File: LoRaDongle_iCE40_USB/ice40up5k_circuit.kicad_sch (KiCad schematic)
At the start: 28 parts, among them IC2 ICE40UP5K-UWG30ITR1K, IC3 N25Q032A13ESC40F, J3 Conn_02x02_Top_Bottom, J6 Conn_01x06, J7 Jumper_NC_Small, J9 Conn_02x02_Top_Bottom, SW1 SW_Push, X1 ECS-2520MV-500-BL-TR

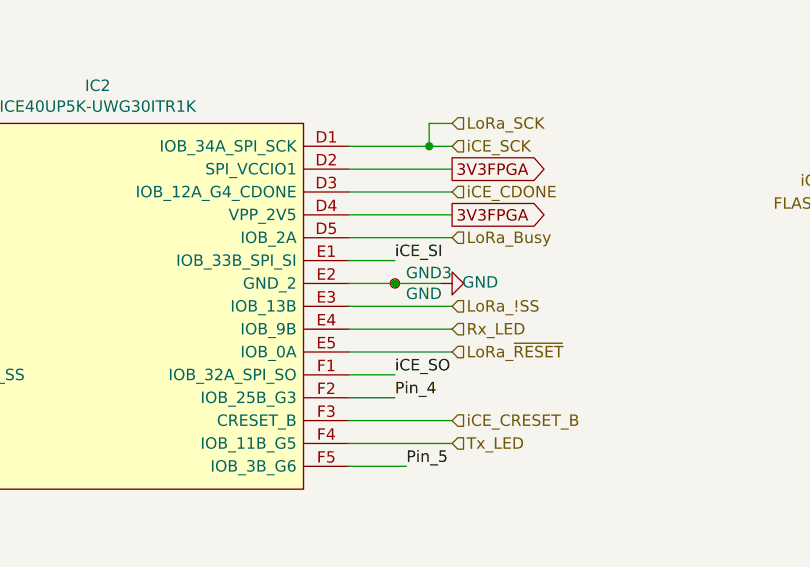
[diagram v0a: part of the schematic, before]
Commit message: added copper pours
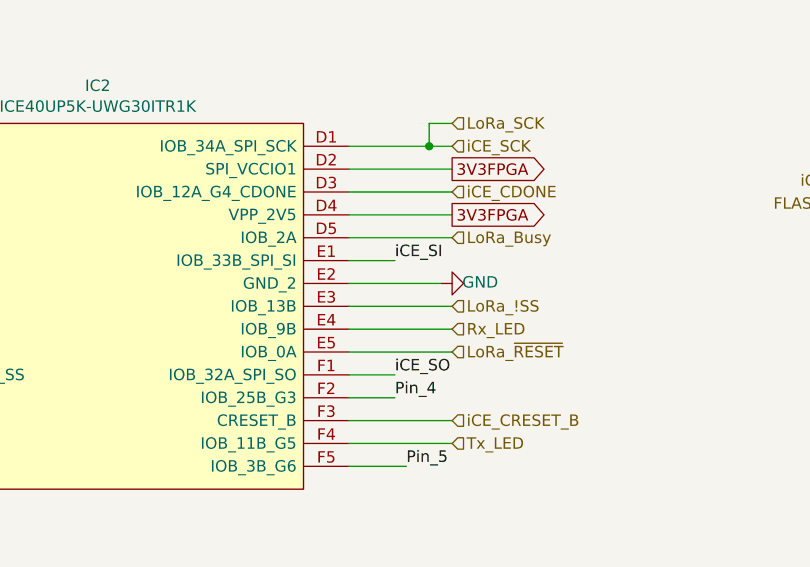
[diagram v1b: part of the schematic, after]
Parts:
- removed GND3: GND, TestPoint:TestPoint_Pad_D1.0mm, symbol Connector:TestPoint_Small
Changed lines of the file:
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@@
   (junction (at 120.65 38.1) (diameter 0) (color 0 0 0 0)
-  )
-  (junction (at 128.27 90.17) (diameter 0) (color 0 0 0 0)
   )
   (junction (at 165.1 39.37) (diameter 0) (color 0 0 0 0)
@@
     (stroke (width 0) (type default) (color 0 0 0 0))
   )
-  (wire (pts (xy 123.19 90.17) (xy 128.27 90.17))
+  (wire (pts (xy 123.19 90.17) (xy 133.35 90.17))
     (stroke (width 0) (type default) (color 0 0 0 0))
   )
@@
   )
   (wire (pts (xy 140.97 157.48) (xy 140.97 153.67))
-    (stroke (width 0) (type default) (color 0 0 0 0))
-  )
-  (wire (pts (xy 128.27 90.17) (xy 133.35 90.17))
     (stroke (width 0) (type default) (color 0 0 0 0))
   )
@@
     (pin "2")
   )
-  (symbol (lib_id "Connector:TestPoint_Small") (at 128.27 90.17 0) (unit 1)
-    (in_bom yes) (on_board yes)
-    (property "Reference" "GND3" (id 0) (at 129.4892 89.0016 0)
-      (effects (font (size 1.27 1.27)) (justify left))
-    )
-    (property "Value" "GND" (id 1) (at 129.4892 91.313 0)
-      (effects (font (size 1.27 1.27)) (justify left))
-    )
-    (property "Footprint" "TestPoint:TestPoint_Pad_D1.0mm" (id 2) (at 133.35 90.17 0)
-      (effects (font (size 1.27 1.27)) hide)
-    )
-    (property "Datasheet" "~" (id 3) (at 133.35 90.17 0)
-      (effects (font (size 1.27 1.27)) hide)
-    )
-    (pin "1")
-  )
 )

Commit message: updating symbol details
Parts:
- C23, C24, C25, C26, C27, C29, C30, C31, C32: Manufacturer (none) -> Murata Electronics; Manufacturer Part Number (none) -> GRM155R71C104KA88D; Package (none) -> 0402; Type (none) -> SMD
- C28: Manufacturer (none) -> Murata Electronics; Manufacturer Part Number (none) -> GRM155R70J105MA12D; Package (none) -> 0402; Type (none) -> SMD
- IC2: Manufacturer (none) -> Lattice Semiconductor; Manufacturer Part Number (none) -> ICE40UP5K-UWG30ITR1K; Package (none) -> 30-UFBGA, WLCSP; Type (none) -> SMD
- J3, J6, J7, J9: Manufacturer (none) -> -; Manufacturer Part Number (none) -> -; Package (none) -> -; Type (none) -> Through Hole
- SW1: Manufacturer (none) -> (none); Type (none) -> Through Hole
- X1: Manufacturer (none) -> ECS Inc.; Manufacturer Part Number (none) -> ECS-2520MV-500-BL-TR; Package (none) -> 4 Pin Crystal; Type (none) -> SMD
- iCE_SI1, iCE_SO1: Manufacturer (none) -> -; Manufacturer Part Number (none) -> -; Package (none) -> -; Type (none) -> -

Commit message: updated BOM
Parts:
- D2: Manufacturer (none) -> SunLED; Manufacturer Part Number (none) -> XZVG53W-8; Package (none) -> 0603
- R13, R14, R15, R16, R17: Manufacturer (none) -> Stackpole Electronics Inc; Manufacturer Part Number (none) -> RMCF0402FT10K0
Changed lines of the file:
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@@
+      (effects (font (size 1.27 1.27)) hide)
+    )
+    (property "Description" "RES 10K OHM 1% 1/16W 0402" (id 4) (at 153.67 149.86 0)
+      (effects (font (size 1.27 1.27)) hide)
+    )
+    (property "Manufacturer" "Stackpole Electronics Inc" (id 5) (at 153.67 149.86 0)
+      (effects (font (size 1.27 1.27)) hide)
+    )
+    (property "Manufacturer Part Number" "RMCF0402FT10K0" (id 6) (at 153.67 149.86 0)
       (effects (font (size 1.27 1.27)) hide)
     )
@@
       (effects (font (size 1.27 1.27)) hide)
     )
+    (property "Description" "LED GREEN CLEAR CHIP SMD" (id 4) (at 140.97 166.37 0)
+      (effects (font (size 1.27 1.27)) hide)
+    )
+    (property "Manufacturer" "SunLED" (id 5) (at 140.97 166.37 0)
+      (effects (font (size 1.27 1.27)) hide)
+    )
+    (property "Manufacturer Part Number" "XZVG53W-8" (id 6) (at 140.97 166.37 0)
+      (effects (font (size 1.27 1.27)) hide)
+    )
+    (property "Package" "0603" (id 7) (at 140.97 166.37 0)
+      (effects (font (size 1.27 1.27)) hide)
+    )
     (pin "1")
     (pin "2")
@@
       (effects (font (size 1.27 1.27)) hide)
     )
+    (property "Description" "RES 10K OHM 1% 1/16W 0402" (id 4) (at 255.27 74.93 0)
+      (effects (font (size 1.27 1.27)) hide)
+    )
+    (property "Manufacturer" "Stackpole Electronics Inc" (id 5) (at 255.27 74.93 0)
+      (effects (font (size 1.27 1.27)) hide)
+    )
+    (property "Manufacturer Part Number" "RMCF0402FT10K0" (id 6) (at 255.27 74.93 0)
+      (effects (font (size 1.27 1.27)) hide)
+    )
     (pin "1")
     (pin "2")
@@
       (effects (font (size 1.27 1.27)) hide)
     )
+    (property "Description" "RES 10K OHM 1% 1/16W 0402" (id 4) (at 250.19 74.93 0)
+      (effects (font (size 1.27 1.27)) hide)
+    )
+    (property "Manufacturer" "Stackpole Electronics Inc" (id 5) (at 250.19 74.93 0)
+      (effects (font (size 1.27 1.27)) hide)
+    )
+    (property "Manufacturer Part Number" "RMCF0402FT10K0" (id 6) (at 250.19 74.93 0)
+      (effects (font (size 1.27 1.27)) hide)
+    )
     (pin "1")
     (pin "2")
@@
       (effects (font (size 1.27 1.27)) hide)
     )
+    (property "Description" "RES 10K OHM 1% 1/16W 0402" (id 4) (at 191.77 83.82 0)
+      (effects (font (size 1.27 1.27)) hide)
+    )
+    (property "Manufacturer" "Stackpole Electronics Inc" (id 5) (at 191.77 83.82 0)
+      (effects (font (size 1.27 1.27)) hide)
+    )
+    (property "Manufacturer Part Number" "RMCF0402FT10K0" (id 6) (at 191.77 83.82 0)
+      (effects (font (size 1.27 1.27)) hide)
+    )
     (pin "1")
     (pin "2")
@@
       (effects (font (size 1.27 1.27)) hide)
     )
+    (property "Description" "RES 10K OHM 1% 1/16W 0402" (id 4) (at 198.12 69.85 0)
+      (effects (font (size 1.27 1.27)) hide)
+    )
+    (property "Manufacturer" "Stackpole Electronics Inc" (id 5) (at 198.12 69.85 0)
+      (effects (font (size 1.27 1.27)) hide)
+    )
+    (property "Manufacturer Part Number" "RMCF0402FT10K0" (id 6) (at 198.12 69.85 0)
+      (effects (font (size 1.27 1.27)) hide)
+    )

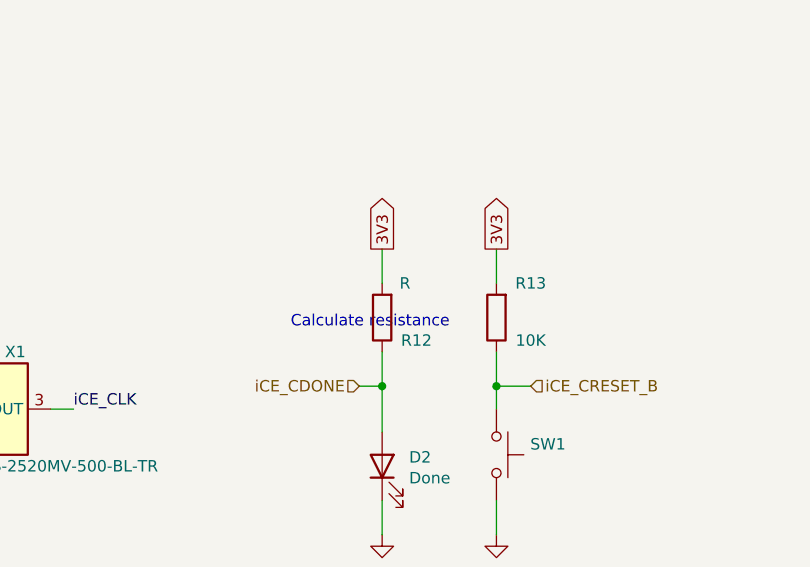
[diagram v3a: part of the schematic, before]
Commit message: generate raw bom csv from kicad
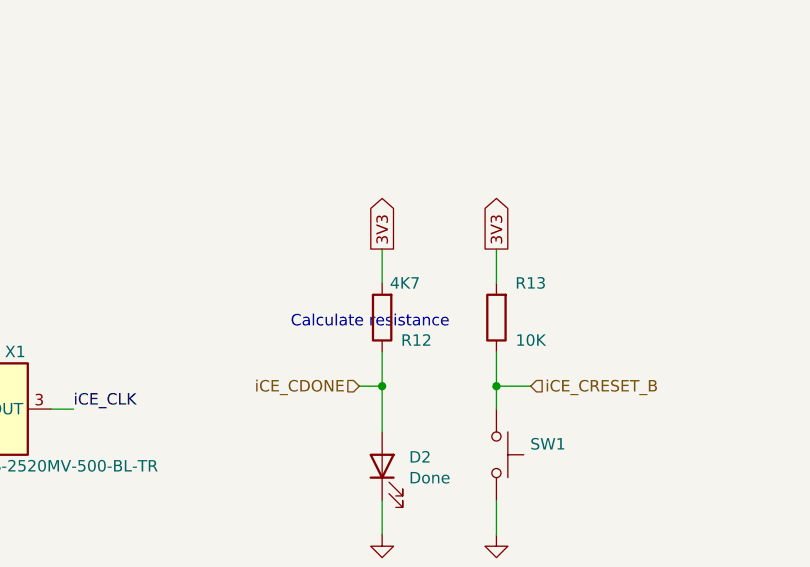
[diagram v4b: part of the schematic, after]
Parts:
- R12: value R -> 4K7; Manufacturer (none) -> Stackpole Electronics Inc; Manufacturer Part Number (none) -> RMCF0402JT4K70; Package (none) -> 0402
- R13, R14, R15, R16, R17: Package (none) -> 0402
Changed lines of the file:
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@@
+      (effects (font (size 1.27 1.27)) hide)
+    )
+    (property "Package" "0402" (id 7) (at 153.67 149.86 0)
       (effects (font (size 1.27 1.27)) hide)
     )
@@
     (in_bom yes) (on_board yes)
     (property "Reference" "R12" (id 0) (at 144.78 152.4 0))
-    (property "Value" "R" (id 1) (at 143.51 146.05 0))
+    (property "Value" "4K7" (id 1) (at 143.51 146.05 0))
     (property "Footprint" "Resistor_SMD:R_0402_1005Metric_Pad0.72x0.64mm_HandSolder" (id 2) (at 142.748 149.86 90)
       (effects (font (size 1.27 1.27)) hide)
     )
     (property "Datasheet" "~" (id 3) (at 140.97 149.86 0)
+      (effects (font (size 1.27 1.27)) hide)
+    )
+    (property "Description" "RES 10K OHM 1% 1/16W 0402" (id 4) (at 140.97 149.86 0)
+      (effects (font (size 1.27 1.27)) hide)
+    )
+    (property "Manufacturer" "Stackpole Electronics Inc" (id 5) (at 140.97 149.86 0)
+      (effects (font (size 1.27 1.27)) hide)
+    )
+    (property "Manufacturer Part Number" "RMCF0402JT4K70" (id 6) (at 140.97 149.86 0)
+      (effects (font (size 1.27 1.27)) hide)
+    )
+    (property "Package" "0402" (id 7) (at 140.97 149.86 0)
       (effects (font (size 1.27 1.27)) hide)
     )
@@
       (effects (font (size 1.27 1.27)) hide)
     )
+    (property "Package" "0402" (id 7) (at 255.27 74.93 0)
+      (effects (font (size 1.27 1.27)) hide)
+    )
     (pin "1")
     (pin "2")
@@
       (effects (font (size 1.27 1.27)) hide)
     )
+    (property "Package" "0402" (id 7) (at 250.19 74.93 0)
+      (effects (font (size 1.27 1.27)) hide)
+    )
     (pin "1")
     (pin "2")
@@
       (effects (font (size 1.27 1.27)) hide)
     )
+    (property "Package" "0402" (id 7) (at 191.77 83.82 0)
+      (effects (font (size 1.27 1.27)) hide)
+    )
     (pin "1")
     (pin "2")
@@
       (effects (font (size 1.27 1.27)) hide)
     )
+    (property "Package" "0402" (id 7) (at 198.12 69.85 0)
+      (effects (font (size 1.27 1.27)) hide)
+    )

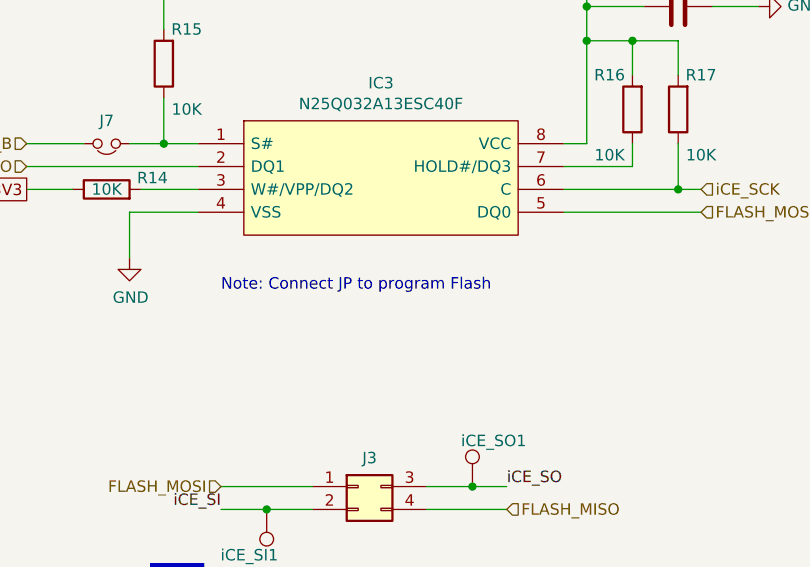
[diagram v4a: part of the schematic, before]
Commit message: update vias and text on schematic
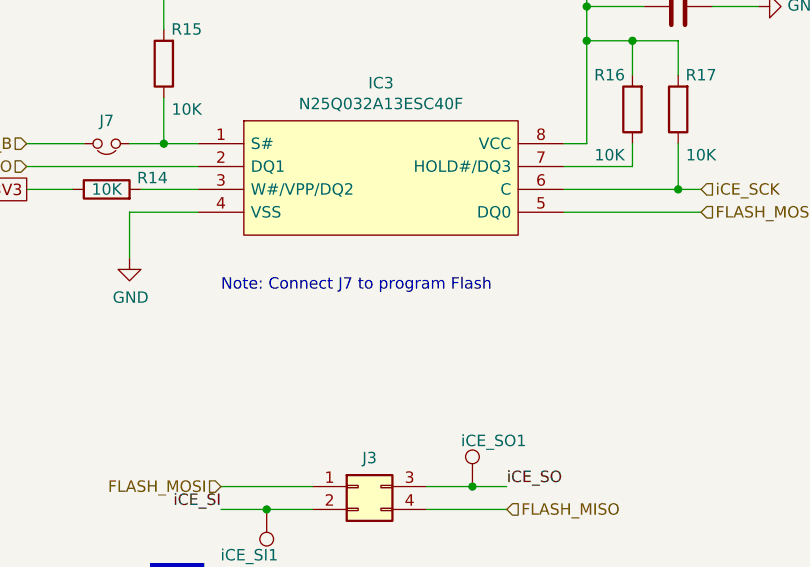
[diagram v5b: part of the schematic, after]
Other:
- note added: "Note: Connect J7 to program Flash"
- note removed: "Note: Connect JP to program Flash"
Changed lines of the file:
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@@
     (effects (font (size 1.27 1.27)) (justify left bottom))
   )
-  (text "Note: Connect JP to program Flash" (at 204.47 95.25 0)
+  (text "Note: Connect J7 to program Flash" (at 204.47 95.25 0)
     (effects (font (size 1.27 1.27)) (justify left bottom))
   )

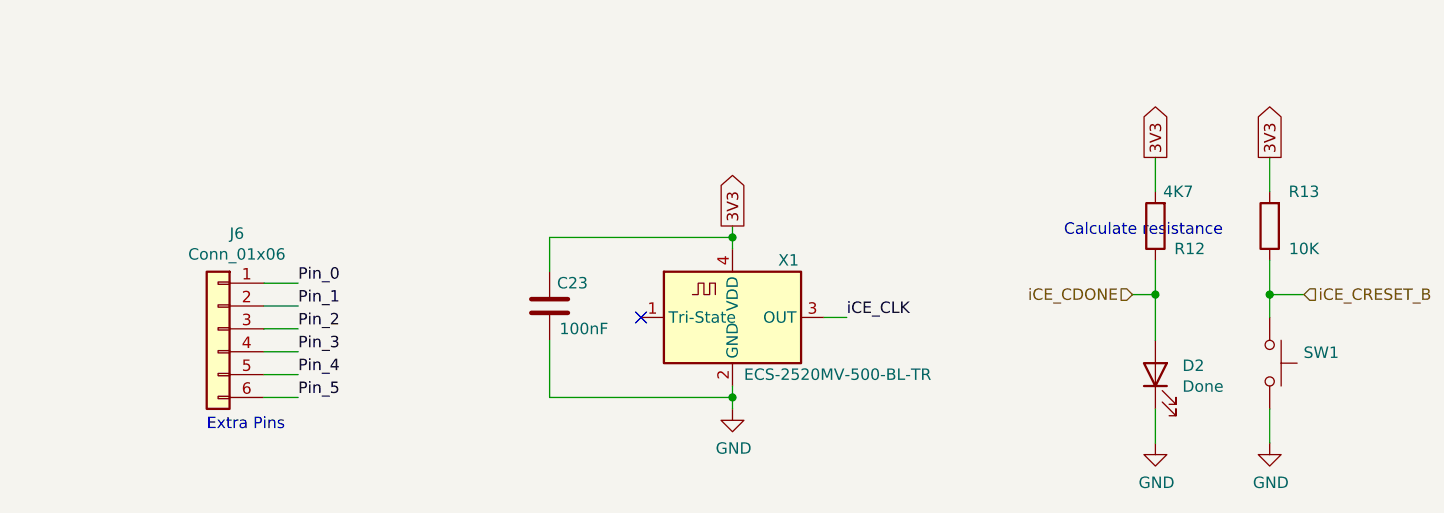
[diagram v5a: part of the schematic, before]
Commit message: added usb flash testpoints & jumper for fpga oscillator
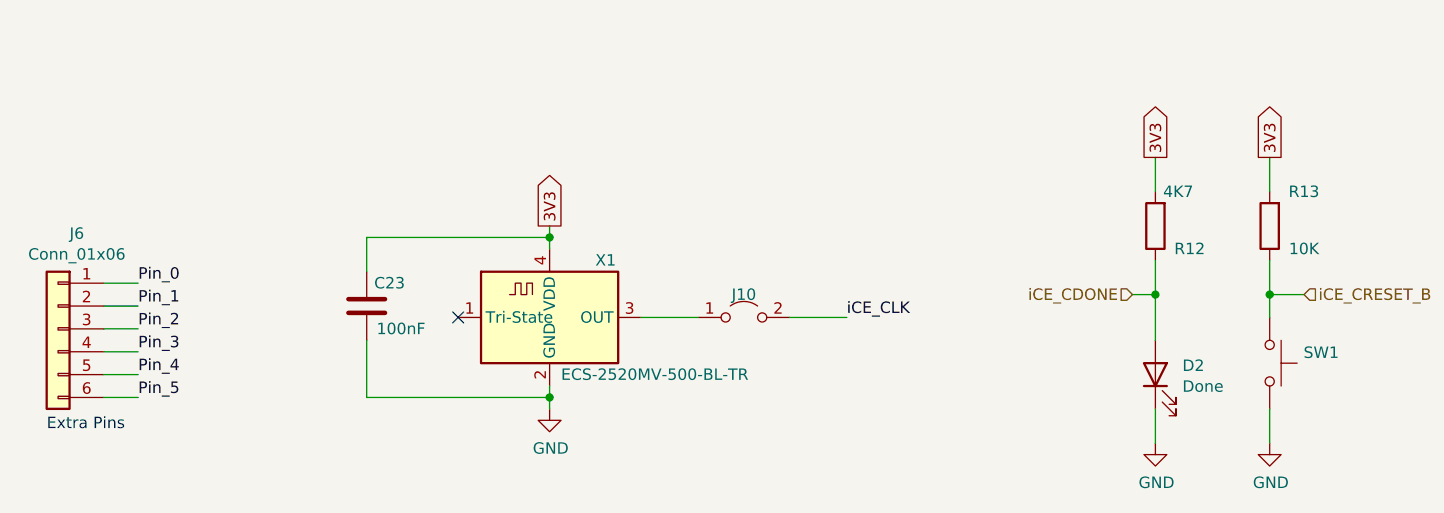
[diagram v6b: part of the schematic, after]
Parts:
- added J10: Jumper_2_Open, Connector_PinHeader_2.54mm:PinHeader_1x02_P2.54mm_Vertical, symbol Jumper:Jumper_2_Open
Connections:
- net iCE_CLK: now also J10.2 (B); no longer X1.3 (OUT)
- new net: J10.1 (A), X1.3 (OUT)
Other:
- note removed: "Calculate resistance"
- moved on the sheet: C23, J6, X1

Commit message: updating silkscreen
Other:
- company: (none) -> Mark Njoroge
- title: (none) -> RiscVLoRaDongle
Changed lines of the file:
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@@
 (kicad_sch (version 20211123) (generator eeschema)
   (paper "A4")
+  (title_block
+    (title "RiscVLoRaDongle")
+    (date "2022-02-03")
+    (rev "1.0")
+    (company "Mark Njoroge")
+  )
   (junction (at 232.41 116.84) (diameter 0) (color 0 0 0 0)
   )

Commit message: completed silkscreen
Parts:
- J10: Manufacturer (none) -> -; Manufacturer Part Number (none) -> -; Package (none) -> -; Type (none) -> Through Hole
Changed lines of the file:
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@@
+      (effects (font (size 1.27 1.27)) hide)
+    )
+    (property "Description" "1x02 Male Header" (id 4) (at 95.25 160.02 0)
+      (effects (font (size 1.27 1.27)) hide)
+    )
+    (property "Manufacturer" "-" (id 5) (at 95.25 160.02 0)
+      (effects (font (size 1.27 1.27)) hide)
+    )
+    (property "Manufacturer Part Number" "-" (id 6) (at 95.25 160.02 0)
+      (effects (font (size 1.27 1.27)) hide)
+    )
+    (property "Package" "-" (id 7) (at 95.25 160.02 0)
+      (effects (font (size 1.27 1.27)) hide)
+    )
+    (property "Type" "Through Hole" (id 8) (at 95.25 160.02 0)
       (effects (font (size 1.27 1.27)) hide)
     )
